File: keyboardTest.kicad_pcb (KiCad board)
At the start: 2 copper layers, 297.8 x 101.2 mm, 12 parts, among them J1 DRAGON_CONNECTION, J2 COCO_CONNECTION

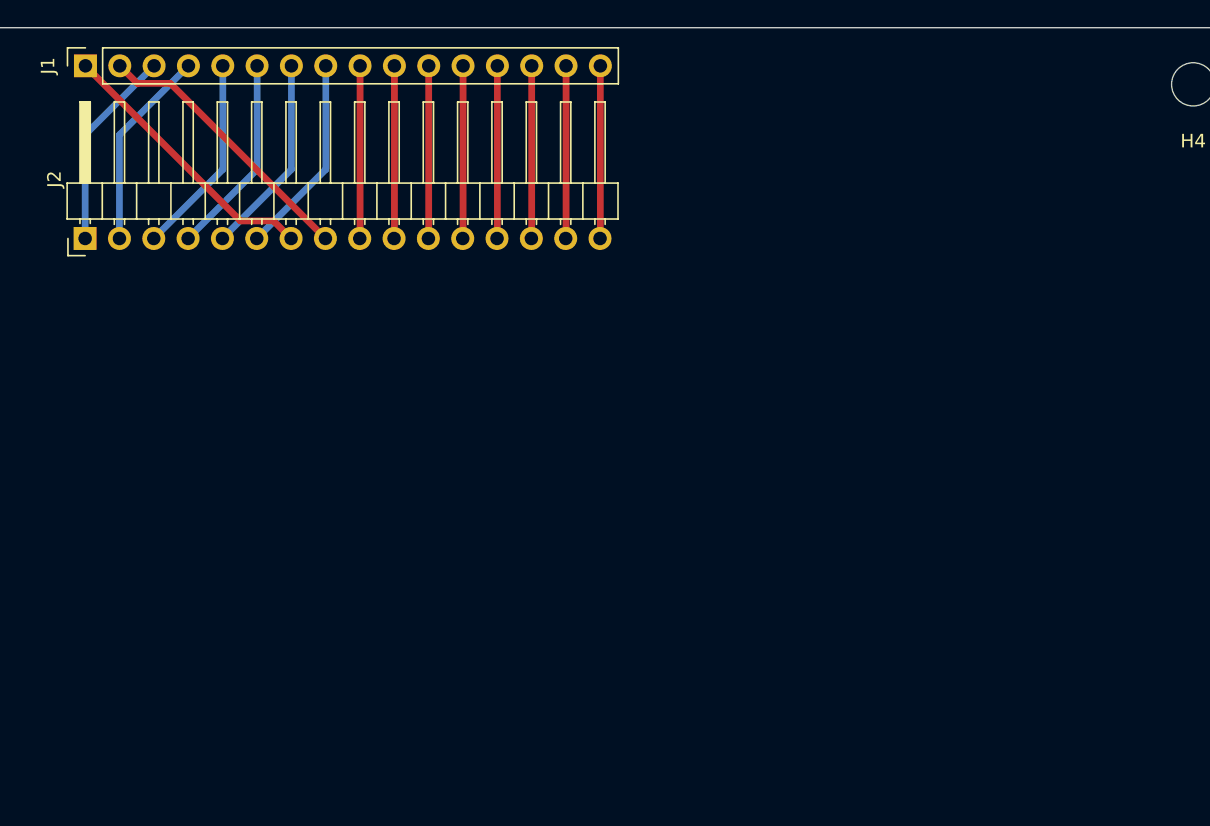
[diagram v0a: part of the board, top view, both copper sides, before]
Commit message: add pico for hid
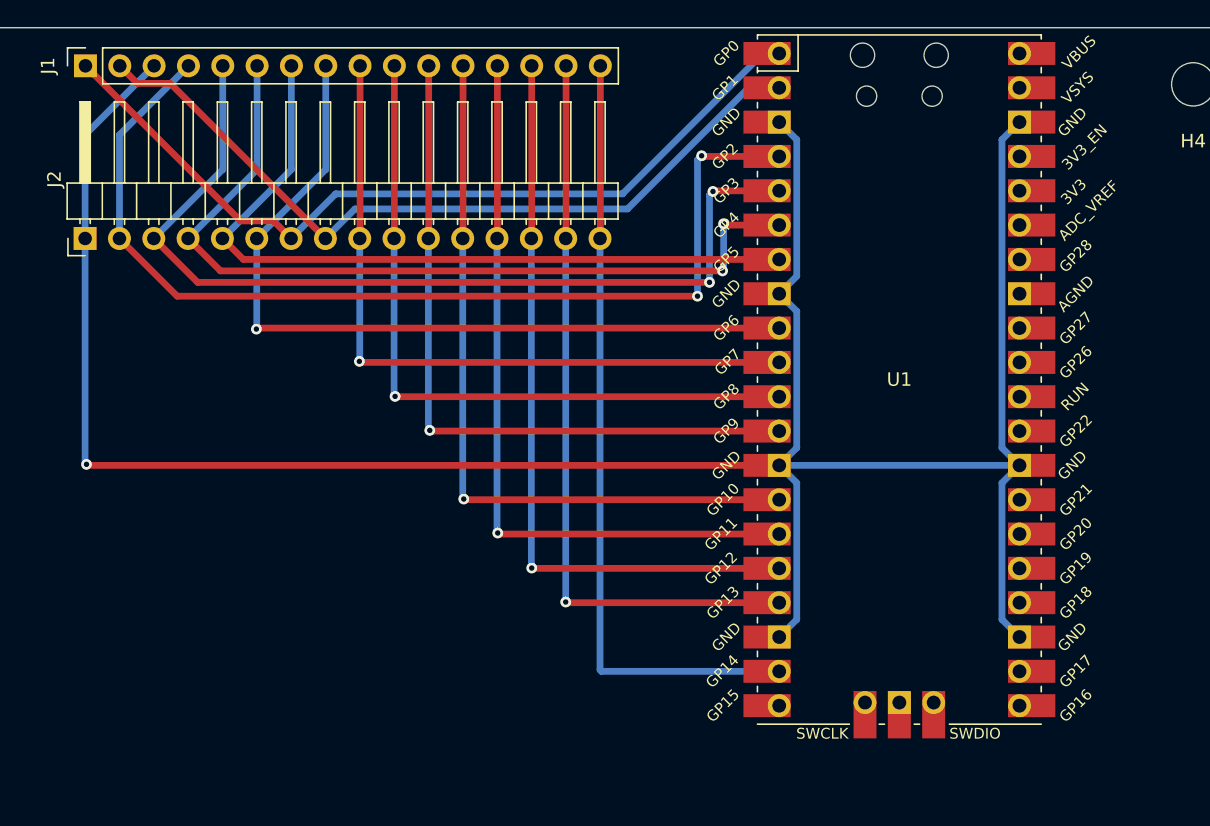
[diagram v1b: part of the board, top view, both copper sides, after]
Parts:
- added U1: Pico, pico:RPi_Pico_SMD_TH, F.Cu at (174.0, 131.3)
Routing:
- net GND: track 14.9 -> 182.3 mm, vias 0 -> 1
- net PA2: track 14.9 -> 75.7 mm, vias 0 -> 2
- net PA3: track 14.9 -> 69.1 mm, vias 0 -> 2
- net PA4: track 14.9 -> 63.1 mm, vias 0 -> 2
- net PA6: track 14.9 -> 60.3 mm, vias 0 -> 1
- net PB7: track 12.8 -> 58.0 mm
- net PB6: track 12.8 -> 55.5 mm, vias 0 -> 1
- net PB5: track 12.8 -> 55.5 mm, vias 0 -> 1
- net PB4: track 12.8 -> 55.5 mm, vias 0 -> 1
- net PB3: track 12.8 -> 55.5 mm, vias 0 -> 1
- net PA5: track 14.9 -> 56.7 mm
- net PA0: track 20.5 -> 62.3 mm
- net PB0: track 12.8 -> 53.0 mm, vias 0 -> 1
- net PB1: track 12.8 -> 52.9 mm, vias 0 -> 1
- net PB2: track 12.8 -> 52.9 mm, vias 0 -> 1
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
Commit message: update board mounting
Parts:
- added H6: MountingHole, MountingHole:MountingHole_3.2mm_M3, F.Cu at (95.7, 148.7)
- turned H3 to 0 degrees
- turned H4 to 0 degrees
- turned H5 to 0 degrees
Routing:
- net GND: track 182.3 -> 172.6 mm, vias 1 -> 0
- net PA2: track 75.7 -> 69.8 mm, vias 2 -> 1
- net PA3: track 69.1 -> 65.3 mm, vias 2 -> 1
- net PA4: track 63.1 -> 61.0 mm, vias 2 -> 1
- net PA6: track 60.3 -> 59.3 mm
- net PB0: track 53.0 -> 52.0 mm
- net PB5: track 55.5 -> 54.5 mm
- net PB6: track 55.5 -> 54.5 mm
- net PB1: track 52.9 -> 52.0 mm
- net PB4: track 55.5 -> 54.5 mm
- net PB3: track 55.5 -> 54.5 mm
- net PB2: track 52.9 -> 52.0 mm

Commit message: reshape board for fit
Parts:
- H1, H2: footprint MountingHole:MountingHole_5.3mm_M5 -> MountingHole:MountingHole_5.3mm_M5_ISO7380_Pad
- moved H1 1.00 mm to (66.4, 156.4)
- moved H2 1.00 mm to (349.0, 176.5)
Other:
- outline, holes or cut-outs redrawn
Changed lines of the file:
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@@
     (pad "" np_thru_hole circle locked (at 0 0) (size 3.2 3.2) (drill 3.2) (layers "*.Cu" "*.Mask"))
   )
-  (footprint "MountingHole:MountingHole_5.3mm_M5" locked (layer "F.Cu")
-    (at 66.3796 155.432)
-    (descr "Mounting Hole 5.3mm, no annular, M5")
-    (tags "mounting hole 5.3mm no annular m5")
+  (footprint "MountingHole:MountingHole_5.3mm_M5_ISO7380_Pad" locked (layer "F.Cu")
+    (at 66.3796 156.432)
+    (descr "Mounting Hole 5.3mm, M5, ISO7380")
+    (tags "mounting hole 5.3mm m5 iso7380")
     (property "Sheetfile" "keyboardTest.kicad_sch")
     (property "Sheetname" "")
@@
     (property "ki_keywords" "mounting hole")
     (attr exclude_from_pos_files exclude_from_bom)
-    (fp_text reference "H1" (at 0 -6.3) (layer "F.SilkS")
-        (effects (font (size 1 1) (thickness 0.15)))
-    )
-    (fp_text value "MountingHole" (at 0 6.3) (layer "F.Fab")
+    (fp_text reference "H1" (at 0 -5.75) (layer "F.SilkS")
+        (effects (font (size 1 1) (thickness 0.15)))
+    )
+    (fp_text value "MountingHole" (at 0 5.75) (layer "F.Fab")
         (effects (font (size 1 1) (thickness 0.15)))
     )
@@
         (effects (font (size 1 1) (thickness 0.15)))
     )
-    (fp_circle (center 0 0) (end 5.3 0)
+    (fp_circle (center 0 0) (end 4.75 0)
       (stroke (width 0.15) (type solid)) (fill none) (layer "Cmts.User"))
-    (fp_circle (center 0 0) (end 5.55 0)
+    (fp_circle (center 0 0) (end 5 0)
       (stroke (width 0.05) (type solid)) (fill none) (layer "F.CrtYd"))
-    (pad "" np_thru_hole circle locked (at 0 0) (size 5.3 5.3) (drill 5.3) (layers "*.Cu" "*.Mask"))
+    (pad "1" thru_hole circle locked (at 0 0) (size 9.5 9.5) (drill 5.3) (layers "*.Cu" "*.Mask"))
   )
   (footprint "pico:RPi_Pico_SMD_TH" (layer "F.Cu")
@@
     (pad "" np_thru_hole circle locked (at 0 0) (size 3.2 3.2) (drill 3.2) (layers "*.Cu" "*.Mask"))
   )
-  (footprint "MountingHole:MountingHole_5.3mm_M5" locked (layer "F.Cu")
-    (at 349 175.4726)
-    (descr "Mounting Hole 5.3mm, no annular, M5")
-    (tags "mounting hole 5.3mm no annular m5")
+  (footprint "MountingHole:MountingHole_5.3mm_M5_ISO7380_Pad" locked (layer "F.Cu")
+    (at 349 176.4726)
+    (descr "Mounting Hole 5.3mm, M5, ISO7380")
+    (tags "mounting hole 5.3mm m5 iso7380")
     (property "Sheetfile" "keyboardTest.kicad_sch")
     (property "Sheetname" "")
@@
     (property "ki_keywords" "mounting hole")
     (attr exclude_from_pos_files exclude_from_bom)
-    (fp_text reference "H2" (at 0 -6.3) (layer "F.SilkS")
-        (effects (font (size 1 1) (thickness 0.15)))
-    )
-    (fp_text value "MountingHole" (at 0 6.3) (layer "F.Fab")
+    (fp_text reference "H2" (at 0 -5.75) (layer "F.SilkS")
+        (effects (font (size 1 1) (thickness 0.15)))
+    )
+    (fp_text value "MountingHole" (at 0 5.75) (layer "F.Fab")
         (effects (font (size 1 1) (thickness 0.15)))
     )
@@
         (effects (font (size 1 1) (thickness 0.15)))
     )
-    (fp_circle (center 0 0) (end 5.3 0)
+    (fp_circle (center 0 0) (end 4.75 0)
       (stroke (width 0.15) (type solid)) (fill none) (layer "Cmts.User"))
-    (fp_circle (center 0 0) (end 5.55 0)
+    (fp_circle (center 0 0) (end 5 0)
       (stroke (width 0.05) (type solid)) (fill none) (layer "F.CrtYd"))
-    (pad "" np_thru_hole circle locked (at 0 0) (size 5.3 5.3) (drill 5.3) (layers "*.Cu" "*.Mask"))
+    (pad "1" thru_hole circle locked (at 0 0) (size 9.5 9.5) (drill 5.3) (layers "*.Cu" "*.Mask"))
   )
   (footprint "MountingHole:MountingHole_3.2mm_M3" locked (layer "F.Cu")
@@
   (gr_line (start 122.936 206.502) (end 121.158 203.5302)
     (stroke (width 0.1) (type default)) (layer "Edge.Cuts"))
-  (gr_line (start 58.2516 203.292355) (end 58.2516 105.537)
+  (gr_line (start 58.2516 203.292355) (end 58.2516 107.1626)
+    (stroke (width 0.1) (type default)) (layer "Edge.Cuts"))
+  (gr_line (start 71.12 106.934) (end 72.898 105.308385)
+    (stroke (width 0.1) (type default)) (layer "Edge.Cuts"))
+  (gr_line (start 343.408 105.307852) (end 344.17 106.172)
     (stroke (width 0.1) (type default)) (layer "Edge.Cuts"))
   (gr_line (start 278.892 206.502) (end 122.936 206.502)
@@
   (gr_line (start 121.158 203.5302) (end 58.4802 203.5302)
     (stroke (width 0.1) (type default)) (layer "Edge.Cuts"))
-  (gr_arc (start 355.871112 105.307837) (mid 356.032757 105.374792) (end 356.099712 105.536437)
-    (stroke (width 0.1) (type default)) (layer "Edge.Cuts"))
-  (gr_arc (start 58.2516 105.537) (mid 58.318555 105.375355) (end 58.4802 105.3084)
-    (stroke (width 0.1) (type default)) (layer "Edge.Cuts"))
-  (gr_line (start 356.099712 105.536437) (end 356.1 203.3016)
+  (gr_arc (start 355.854 106.172) (mid 356.015624 106.238962) (end 356.0826 106.4006)
+    (stroke (width 0.1) (type default)) (layer "Edge.Cuts"))
+  (gr_arc (start 58.2516 107.1626) (mid 58.318555 107.000955) (end 58.4802 106.934)
+    (stroke (width 0.1) (type default)) (layer "Edge.Cuts"))
+  (gr_line (start 356.0826 106.4006) (end 356.1 203.3016)
     (stroke (width 0.1) (type default)) (layer "Edge.Cuts"))
   (gr_arc (start 58.4802 203.5302) (mid 58.316634 203.458629) (end 58.2516 203.292355)
@@
   (gr_line (start 280.162 203.5302) (end 278.892 206.502)
     (stroke (width 0.1) (type default)) (layer "Edge.Cuts"))
-  (gr_line (start 58.4802 105.3084) (end 355.871112 105.307837)
-    (stroke (width 0.1) (type default)) (layer "Edge.Cuts"))
-  (gr_line (start 351.4344 174.4472) (end 346.0242 174.4472)
+  (gr_line (start 58.4802 106.934) (end 71.12 106.934)
+    (stroke (width 0.1) (type default)) (layer "Edge.Cuts"))
+  (gr_line (start 72.898 105.308385) (end 343.408 105.307852)
+    (stroke (width 0.1) (type default)) (layer "Edge.Cuts"))
+  (gr_line (start 344.17 106.172) (end 355.854 106.172)
+    (stroke (width 0.1) (type default)) (layer "Edge.Cuts"))
+  (gr_line (start 351.7011 176.514) (end 346.2909 176.514)
     (stroke (width 0.15) (type default)) (layer "User.8"))
   (gr_line (start 62.6618 203.581) (end 62.6618 105.3338)
     (stroke (width 0.15) (type default)) (layer "User.8"))
+  (gr_line (start 348.996 178.2191) (end 348.996 172.8089)
+    (stroke (width 0.15) (type default)) (layer "User.8"))
   (gr_line (start 57.2516 154.4066) (end 62.6618 154.4066)
+    (stroke (width 0.15) (type default)) (layer "User.8"))
+  (gr_line (start 69.088244 156.435265) (end 63.678044 156.435265)
     (stroke (width 0.15) (type default)) (layer "User.8"))
   (gr_line (start 356.660644 203.568284) (end 356.660644 105.295684)
@@
   (gr_line (start 71.247 105.3084) (end 71.247 203.5048)
     (stroke (width 0.15) (type default)) (layer "User.8"))
+  (gr_line (start 66.383144 152.730165) (end 66.383144 158.140365)
+    (stroke (width 0.15) (type default)) (layer "User.8"))
   (dimension (type aligned) (layer "User.7")
